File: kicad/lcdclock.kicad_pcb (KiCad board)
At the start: 2 copper layers, 41 x 50 mm, 26 parts, among them J1 Conn_JLink_SWD, SW1 SW_Push, U1 STM32L073xx_48, U2 ELV_DCF-2, U3 TPS70630, U4 LCD, Y1 32.768kHz 12.5pF

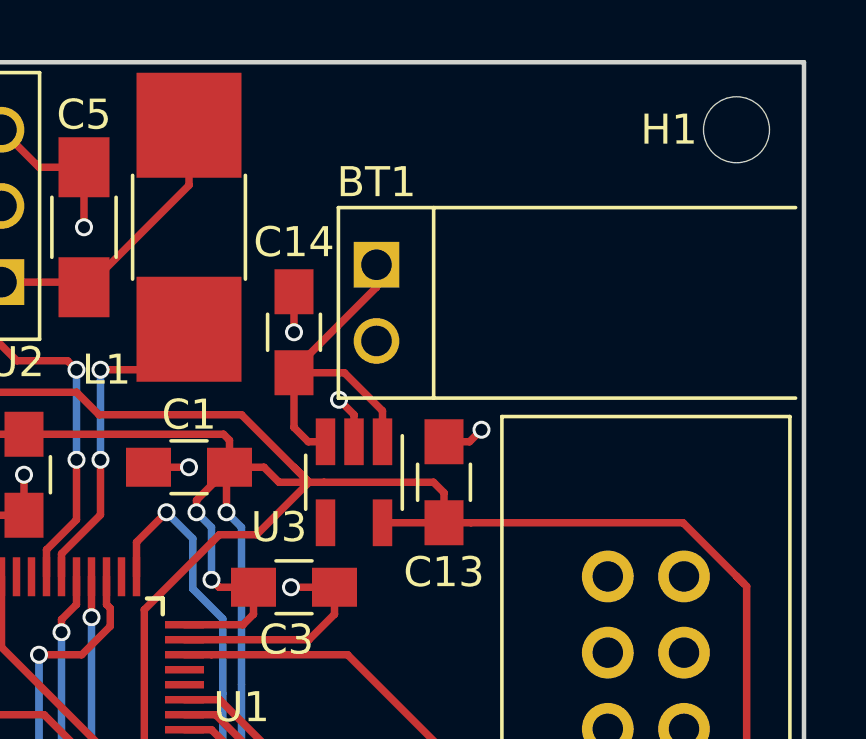
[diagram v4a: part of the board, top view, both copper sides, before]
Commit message: Add reverse voltage protection
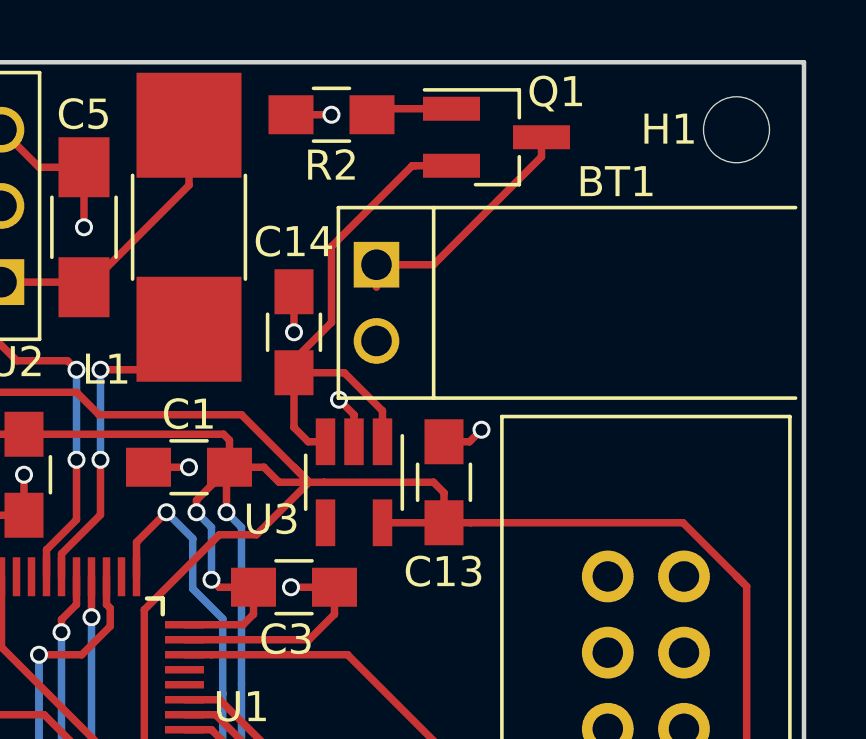
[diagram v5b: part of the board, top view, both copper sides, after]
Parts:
- added Q1: BSH205, TO_SOT_Packages_SMD:SOT-23_Handsoldering, F.Cu at (50.8, 22.5)
- added R2: 100k, Resistors_SMD:R_0805_HandSoldering, F.Cu at (45.2, 21.8)
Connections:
- C14 pad 1: Net-(BT1-Pad1) -> Net-(C14-Pad1)
- U3 pad 1: Net-(BT1-Pad1) -> Net-(C14-Pad1)
- U3 pad 3: Net-(BT1-Pad1) -> Net-(C14-Pad1)
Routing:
- net Net-(C14-Pad1): track 0.00 -> 17.5 mm
- net Net-(BT1-Pad1): track 12.3 -> 8.39 mm
- net Net-(Q1-Pad1): track 0.00 -> 2.73 mm
- net GND: track 44.6 -> 45.9 mm, vias 16 -> 17
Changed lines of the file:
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@@
 (kicad_pcb (version 4) (host pcbnew 4.0.7)
   (general
-    (links 80)
+    (links 83)
     (no_connects 0)
     (area 19.924999 19.924999 61.075001 70.075001)
     (thickness 1.6)
     (drawings 5)
-    (tracks 349)
+    (tracks 361)
     (zones 0)
-    (modules 26)
-    (nets 30)
+    (modules 28)
+    (nets 32)
   )
   (page A4)
@@
   (net 28 "Net-(U1-Pad46)")
   (net 29 "Net-(U1-Pad43)")
+  (net 30 "Net-(C14-Pad1)")
+  (net 31 "Net-(Q1-Pad1)")
   (net_class Default "This is the default net class."
     (clearance 0.2)
@@
     (add_net "Net-(C11-Pad1)")
     (add_net "Net-(C12-Pad1)")
+    (add_net "Net-(C14-Pad1)")
     (add_net "Net-(C5-Pad2)")
     (add_net "Net-(D1-Pad2)")
@@
     (add_net "Net-(J1-Pad9)")
     (add_net "Net-(L1-Pad1)")
+    (add_net "Net-(Q1-Pad1)")
     (add_net "Net-(R1-Pad2)")
     (add_net "Net-(U1-Pad11)")
@@
   (module "LCD Clock:CONNECTOR_2x1" (layer F.Cu)
     (at 46.75 26.75 270)
-    (fp_text reference BT1 (at -2.75 0 360) (layer F.SilkS)
+    (fp_text reference BT1 (at -2.75 -8 360) (layer F.SilkS)
       (effects (font (size 1 1) (thickness 0.15)))
     )
@@
     (fp_line (start 2.35 0.9) (end -2.35 0.9) (layer F.CrtYd) (width 0.05))
     (pad 1 smd rect (at -1.35 0 90) (size 1.5 1.3) (layers F.Cu F.Paste F.Mask)
-      (net 1 "Net-(BT1-Pad1)"))
+      (net 30 "Net-(C14-Pad1)"))
     (pad 2 smd rect (at 1.35 0 90) (size 1.5 1.3) (layers F.Cu F.Paste F.Mask)
       (net 2 GND))
@@
     (tags "SOT-23-5 hand-soldering")
     (attr smd)
-    (fp_text reference U3 (at 1.5 2.5 360) (layer F.SilkS)
+    (fp_text reference U3 (at 1.25 2.75 360) (layer F.SilkS)
       (effects (font (size 1 1) (thickness 0.15)))
     )
@@
     (fp_line (start 2.38 1.8) (end -2.38 1.8) (layer F.CrtYd) (width 0.05))
     (pad 1 smd rect (at -1.35 -0.95 270) (size 1.56 0.65) (layers F.Cu F.Paste F.Mask)
-      (net 1 "Net-(BT1-Pad1)"))
+      (net 30 "Net-(C14-Pad1)"))
     (pad 2 smd rect (at -1.35 0 270) (size 1.56 0.65) (layers F.Cu F.Paste F.Mask)
       (net 2 GND))
     (pad 3 smd rect (at -1.35 0.95 270) (size 1.56 0.65) (layers F.Cu F.Paste F.Mask)
-      (net 1 "Net-(BT1-Pad1)"))
+      (net 30 "Net-(C14-Pad1)"))
     (pad 4 smd rect (at 1.35 0.95 270) (size 1.56 0.65) (layers F.Cu F.Paste F.Mask))
     (pad 5 smd rect (at 1.35 -0.95 270) (size 1.56 0.65) (layers F.Cu F.Paste F.Mask)
@@
     (pad 1 np_thru_hole circle (at 0 0) (size 2.2 2.2) (drill 2.2) (layers *.Cu *.Mask))
   )
+  (module TO_SOT_Packages_SMD:SOT-23_Handsoldering (layer F.Cu)
+    (at 50.75 22.5)
+    (descr "SOT-23, Handsoldering")
+    (tags SOT-23)
+    (attr smd)
+    (fp_text reference Q1 (at 2 -1.5) (layer F.SilkS)
+      (effects (font (size 1 1) (thickness 0.15)))
+    )
+    (fp_text value BSH205 (at 0 2.5) (layer F.Fab)
+      (effects (font (size 1 1) (thickness 0.15)))
+    )
+    (fp_text user %R (at 0 0 90) (layer F.Fab)
+      (effects (font (size 0.5 0.5) (thickness 0.075)))
+    )
+    (fp_line (start 0.76 1.58) (end 0.76 0.65) (layer F.SilkS) (width 0.12))
+    (fp_line (start 0.76 -1.58) (end 0.76 -0.65) (layer F.SilkS) (width 0.12))
+    (fp_line (start -2.7 -1.75) (end 2.7 -1.75) (layer F.CrtYd) (width 0.05))
+    (fp_line (start 2.7 -1.75) (end 2.7 1.75) (layer F.CrtYd) (width 0.05))
+    (fp_line (start 2.7 1.75) (end -2.7 1.75) (layer F.CrtYd) (width 0.05))
+    (fp_line (start -2.7 1.75) (end -2.7 -1.75) (layer F.CrtYd) (width 0.05))
+    (fp_line (start 0.76 -1.58) (end -2.4 -1.58) (layer F.SilkS) (width 0.12))
+    (fp_line (start -0.7 -0.95) (end -0.7 1.5) (layer F.Fab) (width 0.1))
+    (fp_line (start -0.15 -1.52) (end 0.7 -1.52) (layer F.Fab) (width 0.1))
+    (fp_line (start -0.7 -0.95) (end -0.15 -1.52) (layer F.Fab) (width 0.1))
+    (fp_line (start 0.7 -1.52) (end 0.7 1.52) (layer F.Fab) (width 0.1))
+    (fp_line (start -0.7 1.52) (end 0.7 1.52) (layer F.Fab) (width 0.1))
+    (fp_line (start 0.76 1.58) (end -0.7 1.58) (layer F.SilkS) (width 0.12))
+    (pad 1 smd rect (at -1.5 -0.95) (size 1.9 0.8) (layers F.Cu F.Paste F.Mask)
+      (net 31 "Net-(Q1-Pad1)"))
+    (pad 2 smd rect (at -1.5 0.95) (size 1.9 0.8) (layers F.Cu F.Paste F.Mask)
+      (net 30 "Net-(C14-Pad1)"))
+    (pad 3 smd rect (at 1.5 0) (size 1.9 0.8) (layers F.Cu F.Paste F.Mask)
+      (net 1 "Net-(BT1-Pad1)"))
+    (model ${KISYS3DMOD}/TO_SOT_Packages_SMD.3dshapes\SOT-23.wrl
+      (at (xyz 0 0 0))
+      (scale (xyz 1 1 1))
+      (rotate (xyz 0 0 0))
+    )
+  )
+  (module Resistors_SMD:R_0805_HandSoldering (layer F.Cu)
+    (at 45.25 21.75 180)
+    (descr "Resistor SMD 0805, hand soldering")
+    (tags "resistor 0805")
+    (attr smd)
+    (fp_text reference R2 (at 0 -1.7 180) (layer F.SilkS)
+      (effects (font (size 1 1) (thickness 0.15)))
+    )
+    (fp_text value 100k (at 0 1.75 180) (layer F.Fab)
+      (effects (font (size 1 1) (thickness 0.15)))
+    )
+    (fp_text user %R (at 0 0 180) (layer F.Fab)
+      (effects (font (size 0.5 0.5) (thickness 0.075)))
+    )
+    (fp_line (start -1 0.62) (end -1 -0.62) (layer F.Fab) (width 0.1))
+    (fp_line (start 1 0.62) (end -1 0.62) (layer F.Fab) (width 0.1))
+    (fp_line (start 1 -0.62) (end 1 0.62) (layer F.Fab) (width 0.1))
+    (fp_line (start -1 -0.62) (end 1 -0.62) (layer F.Fab) (width 0.1))
+    (fp_line (start 0.6 0.88) (end -0.6 0.88) (layer F.SilkS) (width 0.12))
+    (fp_line (start -0.6 -0.88) (end 0.6 -0.88) (layer F.SilkS) (width 0.12))
+    (fp_line (start -2.35 -0.9) (end 2.35 -0.9) (layer F.CrtYd) (width 0.05))
+    (fp_line (start -2.35 -0.9) (end -2.35 0.9) (layer F.CrtYd) (width 0.05))
+    (fp_line (start 2.35 0.9) (end 2.35 -0.9) (layer F.CrtYd) (width 0.05))
+    (fp_line (start 2.35 0.9) (end -2.35 0.9) (layer F.CrtYd) (width 0.05))
+    (pad 1 smd rect (at -1.35 0 180) (size 1.5 1.3) (layers F.Cu F.Paste F.Mask)
+      (net 31 "Net-(Q1-Pad1)"))
+    (pad 2 smd rect (at 1.35 0 180) (size 1.5 1.3) (layers F.Cu F.Paste F.Mask)
+      (net 2 GND))
+    (model ${KISYS3DMOD}/Resistors_SMD.3dshapes/R_0805.wrl
+      (at (xyz 0 0 0))
+      (scale (xyz 1 1 1))
+      (rotate (xyz 0 0 0))
+    )
+  )
   (gr_line (start 61 20) (end 20 20) (layer Edge.Cuts) (width 0.15))
   (gr_line (start 61 70) (end 61 20) (layer Edge.Cuts) (width 0.15))
@@
   (gr_line (start 20 70) (end 60.75 70) (layer Edge.Cuts) (width 0.15))
   (gr_line (start 20 20) (end 20 70) (layer Edge.Cuts) (width 0.15))
-  (segment (start 44 30.35) (end 45.68 30.35) (width 0.25) (layer F.Cu) (net 1))
-  (segment (start 45.68 30.35) (end 46.95 31.62) (width 0.25) (layer F.Cu) (net 1))
-  (segment (start 46.95 31.62) (end 46.95 32.65) (width 0.25) (layer F.Cu) (net 1))
-  (segment (start 44 30.35) (end 44 30.25) (width 0.25) (layer F.Cu) (net 1))
-  (segment (start 44 30.25) (end 46.75 27.5) (width 0.25) (layer F.Cu) (net 1))
+  (segment (start 46.75 26.75) (end 48.65 26.75) (width 0.25) (layer F.Cu) (net 1))
+  (segment (start 48.65 26.75) (end 52.25 23.15) (width 0.25) (layer F.Cu) (net 1))
+  (segment (start 52.25 23.15) (end 52.25 22.5) (width 0.25) (layer F.Cu) (net 1))
   (segment (start 46.75 27.5) (end 46.75 26.75) (width 0.25) (layer F.Cu) (net 1))
-  (segment (start 44 30.35) (end 44 32.175) (width 0.25) (layer F.Cu) (net 1))
-  (segment (start 44 32.175) (end 44.475 32.65) (width 0.25) (layer F.Cu) (net 1))
-  (segment (start 44.475 32.65) (end 45.05 32.65) (width 0.25) (layer F.Cu) (net 1))
+  (segment (start 43.9 21.75) (end 45.25 21.75) (width 0.25) (layer F.Cu) (net 2))
+  (via (at 45.25 21.75) (size 0.6) (drill 0.4) (layers F.Cu B.Cu) (net 2))
   (segment (start 46 32.65) (end 46 31.75) (width 0.25) (layer F.Cu) (net 2))
   (segment (start 46 31.75) (end 45.5 31.25) (width 0.25) (layer F.Cu) (net 2))
@@
   (segment (start 35.75 37.15) (end 35.75 36.25) (width 0.25) (layer F.Cu) (net 29))
   (segment (start 35.75 36.25) (end 36.75 35.25) (width 0.25) (layer F.Cu) (net 29))
+  (segment (start 45.25 28.675002) (end 45.25 26.140998) (width 0.25) (layer F.Cu) (net 30))
+  (segment (start 45.25 26.140998) (end 47.940998 23.45) (width 0.25) (layer F.Cu) (net 30))
+  (segment (start 47.940998 23.45) (end 48.05 23.45) (width 0.25) (layer F.Cu) (net 30))
+  (segment (start 48.05 23.45) (end 49.25 23.45) (width 0.25) (layer F.Cu) (net 30))
+  (segment (start 44 30.35) (end 44 29.925002) (width 0.25) (layer F.Cu) (net 30))
+  (segment (start 44 29.925002) (end 45.25 28.675002) (width 0.25) (layer F.Cu) (net 30))
+  (segment (start 44 30.35) (end 45.68 30.35) (width 0.25) (layer F.Cu) (net 30))
+  (segment (start 45.68 30.35) (end 46.95 31.62) (width 0.25) (layer F.Cu) (net 30))
+  (segment (start 46.95 31.62) (end 46.95 32.65) (width 0.25) (layer F.Cu) (net 30))
+  (segment (start 44 30.35) (end 44 30.25) (width 0.25) (layer F.Cu) (net 30))
+  (segment (start 44 30.35) (end 44 32.175) (width 0.25) (layer F.Cu) (net 30))
+  (segment (start 44 32.175) (end 44.475 32.65) (width 0.25) (layer F.Cu) (net 30))
+  (segment (start 44.475 32.65) (end 45.05 32.65) (width 0.25) (layer F.Cu) (net 30))
+  (segment (start 49.25 21.55) (end 46.8 21.55) (width 0.25) (layer F.Cu) (net 31))
+  (segment (start 46.8 21.55) (end 46.6 21.75) (width 0.25) (layer F.Cu) (net 31))
   (zone (net 2) (net_name GND) (layer B.Cu) (hatch edge 0.508)
     (connect_pads (clearance 0.508))

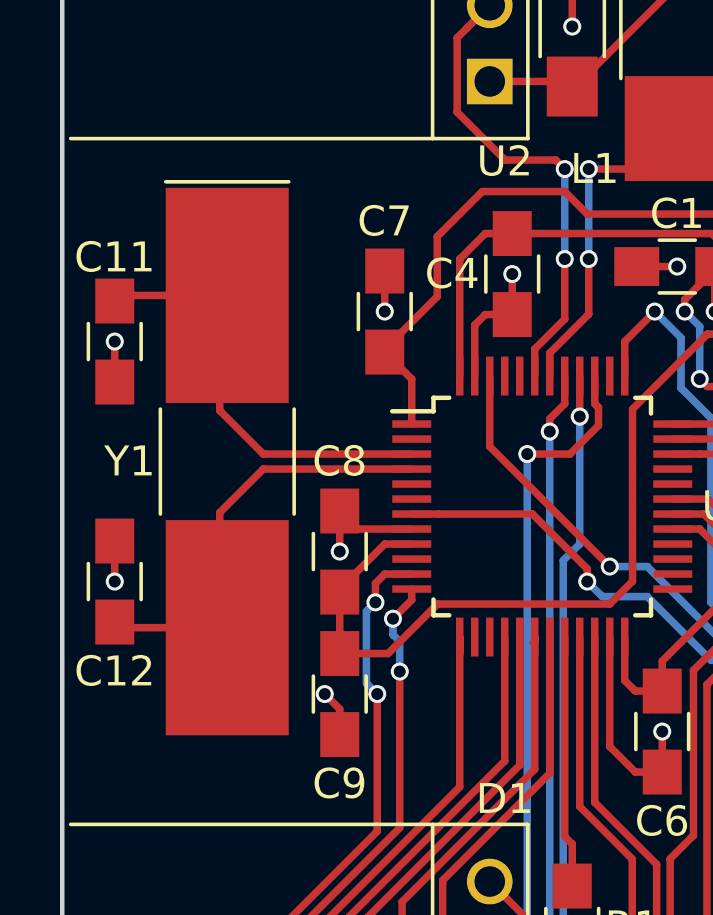
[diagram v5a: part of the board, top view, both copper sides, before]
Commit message: Replace crystal Y1 footprint with a smaller one
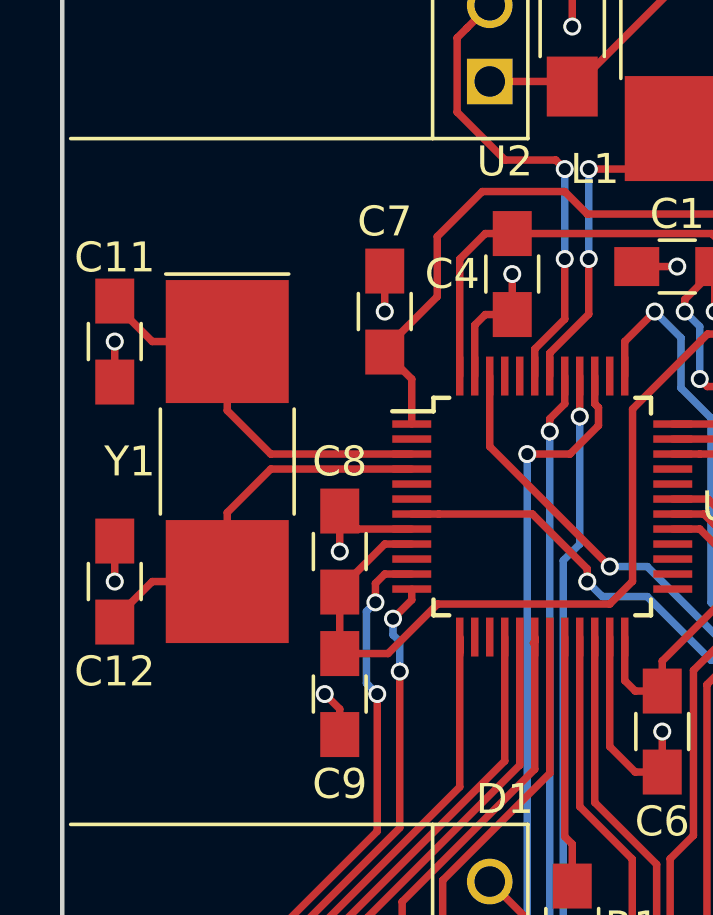
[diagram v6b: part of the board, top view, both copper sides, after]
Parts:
- Y1: footprint Crystals:Crystal_SMD_SeikoEpson_MC405-2pin_9.6x4.1mm_HandSoldering -> Crystals:Crystal_SMD_SeikoEpson_MC405-2pin_9.6x4.1mm
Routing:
- net Net-(C12-Pad1): track 14.4 -> 13.7 mm
- net Net-(C11-Pad1): track 16.0 -> 15.2 mm
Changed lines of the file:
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@@
     (thickness 1.6)
     (drawings 5)
-    (tracks 361)
+    (tracks 364)
     (zones 0)
     (modules 28)
@@
       (net 24 "Net-(U1-Pad31)"))
   )
-  (module Crystals:Crystal_SMD_SeikoEpson_MC405-2pin_9.6x4.1mm_HandSoldering (layer F.Cu)
-    (at 25.5 40 270)
-    (descr "SMD Crystal Seiko Epson MC-405 https://support.epson.biz/td/api/doc_check.php?dl=brief_MC-306_en.pdf, hand-soldering, 9.6x4.1mm^2 package")
-    (tags "SMD SMT crystal hand-soldering")
-    (attr smd)
-    (fp_text reference Y1 (at 0 3.25 360) (layer F.SilkS)
-      (effects (font (size 1 1) (thickness 0.15)))
-    )
-    (fp_text value "32.768kHz 12.5pF" (at 0 3.23 270) (layer F.Fab)
-      (effects (font (size 1 1) (thickness 0.15)))
-    )
-    (fp_text user %R (at 0 0 270) (layer F.Fab)
-      (effects (font (size 1 1) (thickness 0.15)))
-    )
-    (fp_line (start -4.8 -2.03) (end -4.8 2.03) (layer F.Fab) (width 0.1))
-    (fp_line (start -4.8 2.03) (end 4.8 2.03) (layer F.Fab) (width 0.1))
-    (fp_line (start 4.8 2.03) (end 4.8 -2.03) (layer F.Fab) (width 0.1))
-    (fp_line (start 4.8 -2.03) (end -4.8 -2.03) (layer F.Fab) (width 0.1))
-    (fp_line (start -4.8 1.03) (end -3.8 2.03) (layer F.Fab) (width 0.1))
-    (fp_line (start -1.75 -2.23) (end 1.75 -2.23) (layer F.SilkS) (width 0.12))
-    (fp_line (start -1.75 2.23) (end 1.75 2.23) (layer F.SilkS) (width 0.12))
-    (fp_line (start -9.325 -2.05) (end -9.325 2.05) (layer F.SilkS) (width 0.12))
-    (fp_line (start -9.4 -2.3) (end -9.4 2.3) (layer F.CrtYd) (width 0.05))
-    (fp_line (start -9.4 2.3) (end 9.4 2.3) (layer F.CrtYd) (width 0.05))
-    (fp_line (start 9.4 2.3) (end 9.4 -2.3) (layer F.CrtYd) (width 0.05))
-    (fp_line (start 9.4 -2.3) (end -9.4 -2.3) (layer F.CrtYd) (width 0.05))
-    (pad 1 smd rect (at -5.5375 0 270) (size 7.175 4.1) (layers F.Cu F.Paste F.Mask)
-      (net 7 "Net-(C11-Pad1)"))
-    (pad 2 smd rect (at 5.5375 0 270) (size 7.175 4.1) (layers F.Cu F.Paste F.Mask)
-      (net 8 "Net-(C12-Pad1)"))
-    (model ${KISYS3DMOD}/Crystals.3dshapes/Crystal_SMD_SeikoEpson_MC405-2pin_9.6x4.1mm_HandSoldering.wrl
-      (at (xyz 0 0 0))
-      (scale (xyz 1 1 1))
-      (rotate (xyz 0 0 0))
-    )
-  )
   (module Mounting_Holes:MountingHole_2.2mm_M2 (layer F.Cu)
     (at 58.75 22.25)
@@
       (net 2 GND))
     (model ${KISYS3DMOD}/Resistors_SMD.3dshapes/R_0805.wrl
+      (at (xyz 0 0 0))
+      (scale (xyz 1 1 1))
+      (rotate (xyz 0 0 0))
+    )
+  )
+  (module Crystals:Crystal_SMD_SeikoEpson_MC405-2pin_9.6x4.1mm (layer F.Cu)
+    (at 25.5 40 270)
+    (descr "SMD Crystal Seiko Epson MC-405 https://support.epson.biz/td/api/doc_check.php?dl=brief_MC-306_en.pdf, 9.6x4.1mm^2 package")
+    (tags "SMD SMT crystal")
+    (attr smd)
+    (fp_text reference Y1 (at 0 3.25 360) (layer F.SilkS)
+      (effects (font (size 1 1) (thickness 0.15)))
+    )
+    (fp_text value "32.768kHz 12.5pF" (at 0 3.23 270) (layer F.Fab)
+      (effects (font (size 1 1) (thickness 0.15)))
+    )
+    (fp_text user %R (at 0 0 270) (layer F.Fab)
+      (effects (font (size 1 1) (thickness 0.15)))
+    )
+    (fp_line (start -4.8 -2.03) (end -4.8 2.03) (layer F.Fab) (width 0.1))
+    (fp_line (start -4.8 2.03) (end 4.8 2.03) (layer F.Fab) (width 0.1))
+    (fp_line (start 4.8 2.03) (end 4.8 -2.03) (layer F.Fab) (width 0.1))
+    (fp_line (start 4.8 -2.03) (end -4.8 -2.03) (layer F.Fab) (width 0.1))
+    (fp_line (start -4.8 1.03) (end -3.8 2.03) (layer F.Fab) (width 0.1))
+    (fp_line (start -1.75 -2.23) (end 1.75 -2.23) (layer F.SilkS) (width 0.12))
+    (fp_line (start -1.75 2.23) (end 1.75 2.23) (layer F.SilkS) (width 0.12))
+    (fp_line (start -6.25 -2.05) (end -6.25 2.05) (layer F.SilkS) (width 0.12))
+    (fp_line (start -6.3 -2.3) (end -6.3 2.3) (layer F.CrtYd) (width 0.05))
+    (fp_line (start -6.3 2.3) (end 6.3 2.3) (layer F.CrtYd) (width 0.05))
+    (fp_line (start 6.3 2.3) (end 6.3 -2.3) (layer F.CrtYd) (width 0.05))
+    (fp_line (start 6.3 -2.3) (end -6.3 -2.3) (layer F.CrtYd) (width 0.05))
+    (pad 1 smd rect (at -4 0 270) (size 4.1 4.1) (layers F.Cu F.Paste F.Mask)
+      (net 7 "Net-(C11-Pad1)"))
+    (pad 2 smd rect (at 4 0 270) (size 4.1 4.1) (layers F.Cu F.Paste F.Mask)
+      (net 8 "Net-(C12-Pad1)"))
+    (model ${KISYS3DMOD}/Crystals.3dshapes/Crystal_SMD_SeikoEpson_MC405-2pin_9.6x4.1mm.wrl
       (at (xyz 0 0 0))
       (scale (xyz 1 1 1))
@@
   (segment (start 32.55 41.75) (end 31.65 41.75) (width 0.25) (layer F.Cu) (net 6))
   (segment (start 37.5 44) (end 37.5 43.575736) (width 0.25) (layer F.Cu) (net 6))
-  (segment (start 31.65 39.75) (end 26.75 39.75) (width 0.25) (layer F.Cu) (net 7))
-  (segment (start 25.25 34.4625) (end 25.25 38.3) (width 0.25) (layer F.Cu) (net 7))
-  (segment (start 25.25 38.3) (end 26.7 39.75) (width 0.25) (layer F.Cu) (net 7))
-  (segment (start 26.7 39.75) (end 26.75 39.75) (width 0.25) (layer F.Cu) (net 7))
-  (segment (start 25.25 34.4625) (end 21.9375 34.4625) (width 0.25) (layer F.Cu) (net 7))
+  (segment (start 25.5 36) (end 23 36) (width 0.25) (layer F.Cu) (net 7))
+  (segment (start 23 36) (end 21.75 34.75) (width 0.25) (layer F.Cu) (net 7))
+  (segment (start 21.75 34.75) (end 21.75 34.65) (width 0.25) (layer F.Cu) (net 7))
+  (segment (start 31.65 39.75) (end 26.95 39.75) (width 0.25) (layer F.Cu) (net 7))
+  (segment (start 26.95 39.75) (end 25.5 38.3) (width 0.25) (layer F.Cu) (net 7))
+  (segment (start 25.5 38.3) (end 25.5 36) (width 0.25) (layer F.Cu) (net 7))
   (segment (start 21.9375 34.4625) (end 21.75 34.65) (width 0.25) (layer F.Cu) (net 7))
   (segment (start 25.25 36) (end 25.25 34.4625) (width 0.25) (layer F.Cu) (net 7))
-  (segment (start 31.65 40.25) (end 26.7 40.25) (width 0.25) (layer F.Cu) (net 8))
-  (segment (start 25.25 41.7) (end 25.25 45.5375) (width 0.25) (layer F.Cu) (net 8))
-  (segment (start 26.7 40.25) (end 25.25 41.7) (width 0.25) (layer F.Cu) (net 8))
-  (segment (start 25.25 45.5375) (end 21.9375 45.5375) (width 0.25) (layer F.Cu) (net 8))
+  (segment (start 25.5 44) (end 23 44) (width 0.25) (layer F.Cu) (net 8))
+  (segment (start 23 44) (end 21.75 45.25) (width 0.25) (layer F.Cu) (net 8))
+  (segment (start 21.75 45.25) (end 21.75 45.35) (width 0.25) (layer F.Cu) (net 8))
+  (segment (start 31.65 40.25) (end 26.95 40.25) (width 0.25) (layer F.Cu) (net 8))
+  (segment (start 26.95 40.25) (end 25.5 41.7) (width 0.25) (layer F.Cu) (net 8))
+  (segment (start 25.5 41.7) (end 25.5 44) (width 0.25) (layer F.Cu) (net 8))
   (segment (start 21.9375 45.5375) (end 21.75 45.35) (width 0.25) (layer F.Cu) (net 8))
   (segment (start 37 56.85) (end 37 56.75) (width 0.25) (layer F.Cu) (net 9))
